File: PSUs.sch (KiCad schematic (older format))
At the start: 27 parts, among them U1 LM2674N-ADJ, U11 MCP4151-103E/P, U12 MCP4151-103E/P, U2 LM2574N-3.3, U3 LM2674N-ADJ

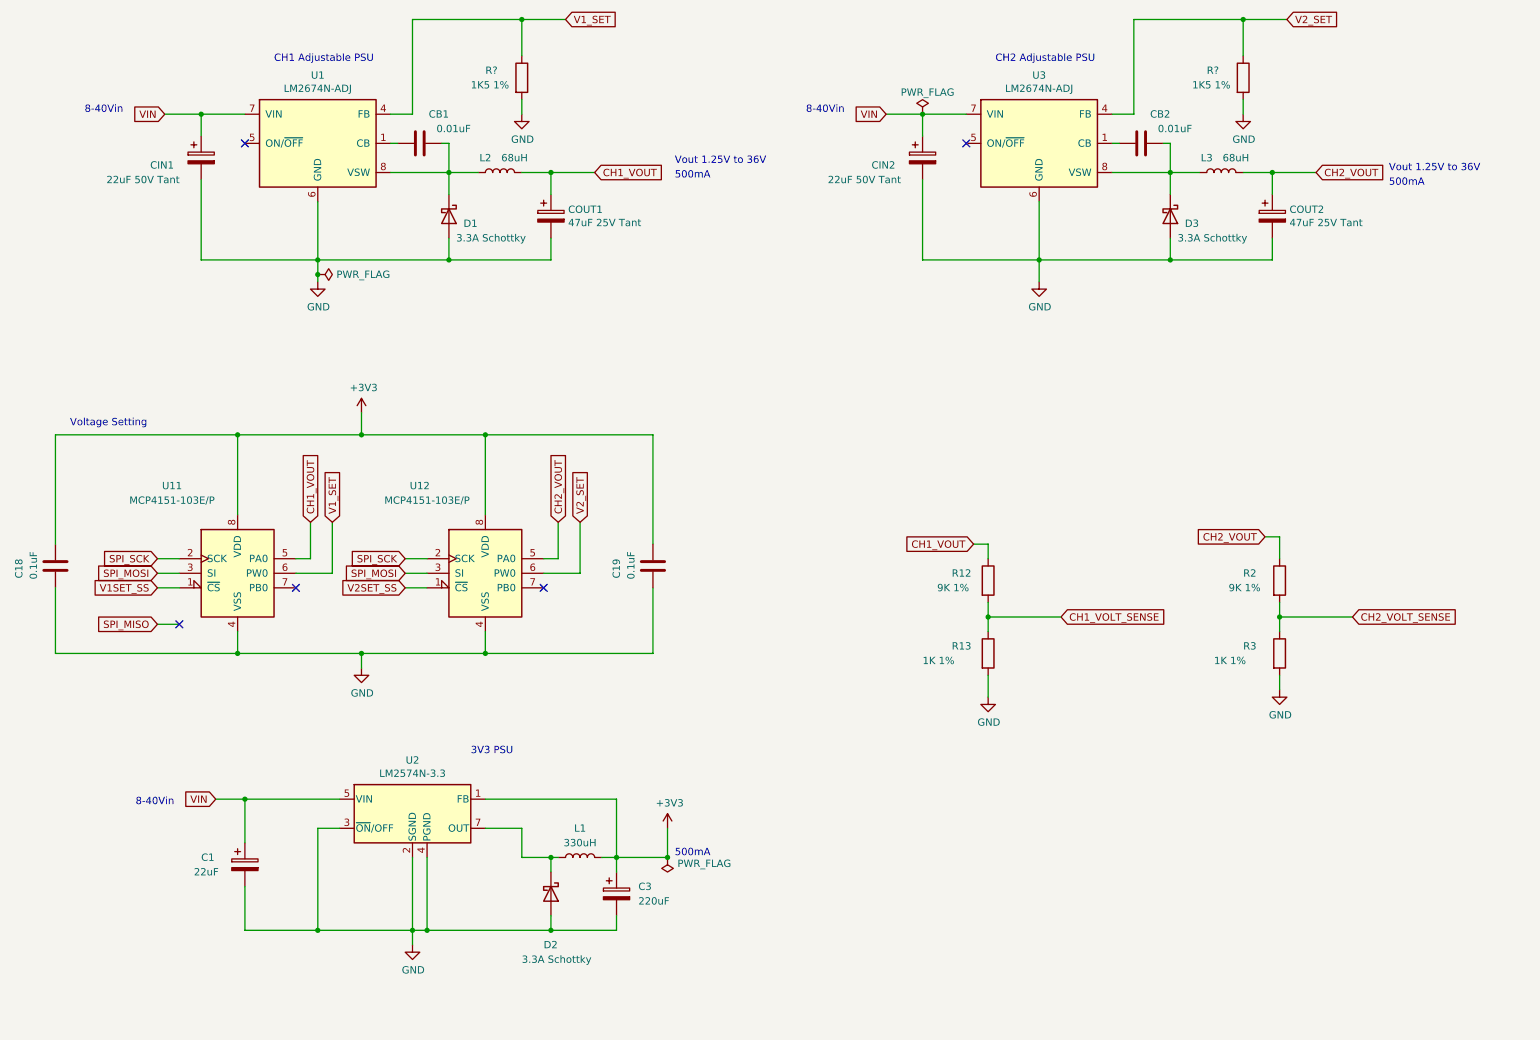
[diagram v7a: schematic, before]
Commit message: Added capacitance multiplier for reducing psu ripple. Settled on 1 decimal place Voltage adjustment, not the best but we can't seem to get the ADC to settle down
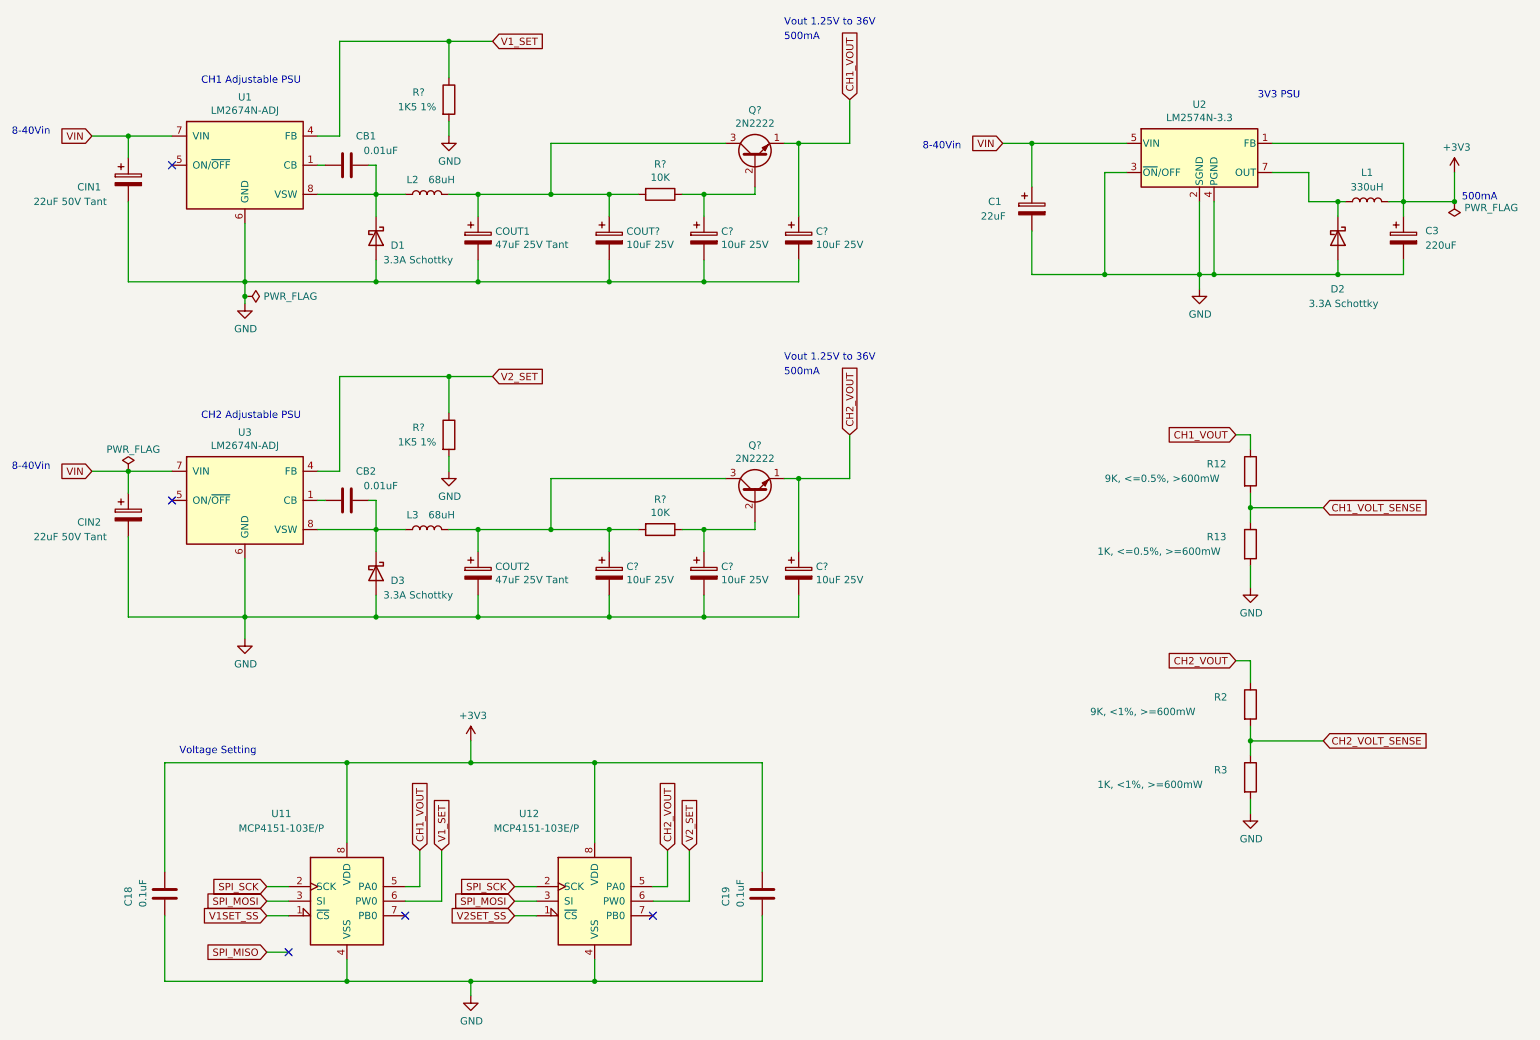
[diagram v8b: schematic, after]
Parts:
- added C? (x6): 10uF 25V, symbol Device:CP
- added Q? (x2): 2N2222, Package_TO_SOT_THT:TO-39-3, symbol Transistor_BJT:2N2219
- added R? (x2): 10K, symbol Device:R
- R12: value 9K 1% -> 9K, <=0.5%, >600mW
- R13: value 1K 1% -> 1K, <=0.5%, >=600mW
- R2: value 9K 1% -> 9K, <1%, >=600mW
- R3: value 1K 1% -> 1K, <1%, >=600mW
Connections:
- net CH1_VOUT: now also C?.1, Q?.1 (E); no longer COUT1.1, L2.2
- net CH2_VOUT: now also C?.1, Q?.1 (E); no longer COUT2.1, L3.2
- net GND: now also C?.2, C?.2, C?.2, C?.2, C?.2, C?.2
- new net: C?.1, Q?.2 (B), R?.1 (x2)
- new net: C?.1, COUT1.1, L2.2, Q?.3 (C), R?.2
- new net: C?.1, COUT2.1, L3.2, Q?.3 (C), R?.2
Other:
- moved on the sheet: C1, C18, C19, C3, CB1, CB2, CIN1, CIN2, COUT1, COUT2, D1, D2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
